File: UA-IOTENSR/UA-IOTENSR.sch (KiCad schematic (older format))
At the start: 4 parts, among them SW101 SW_MEC_5G, U101 ESP32-S2-WROOM, U102 SCD4X

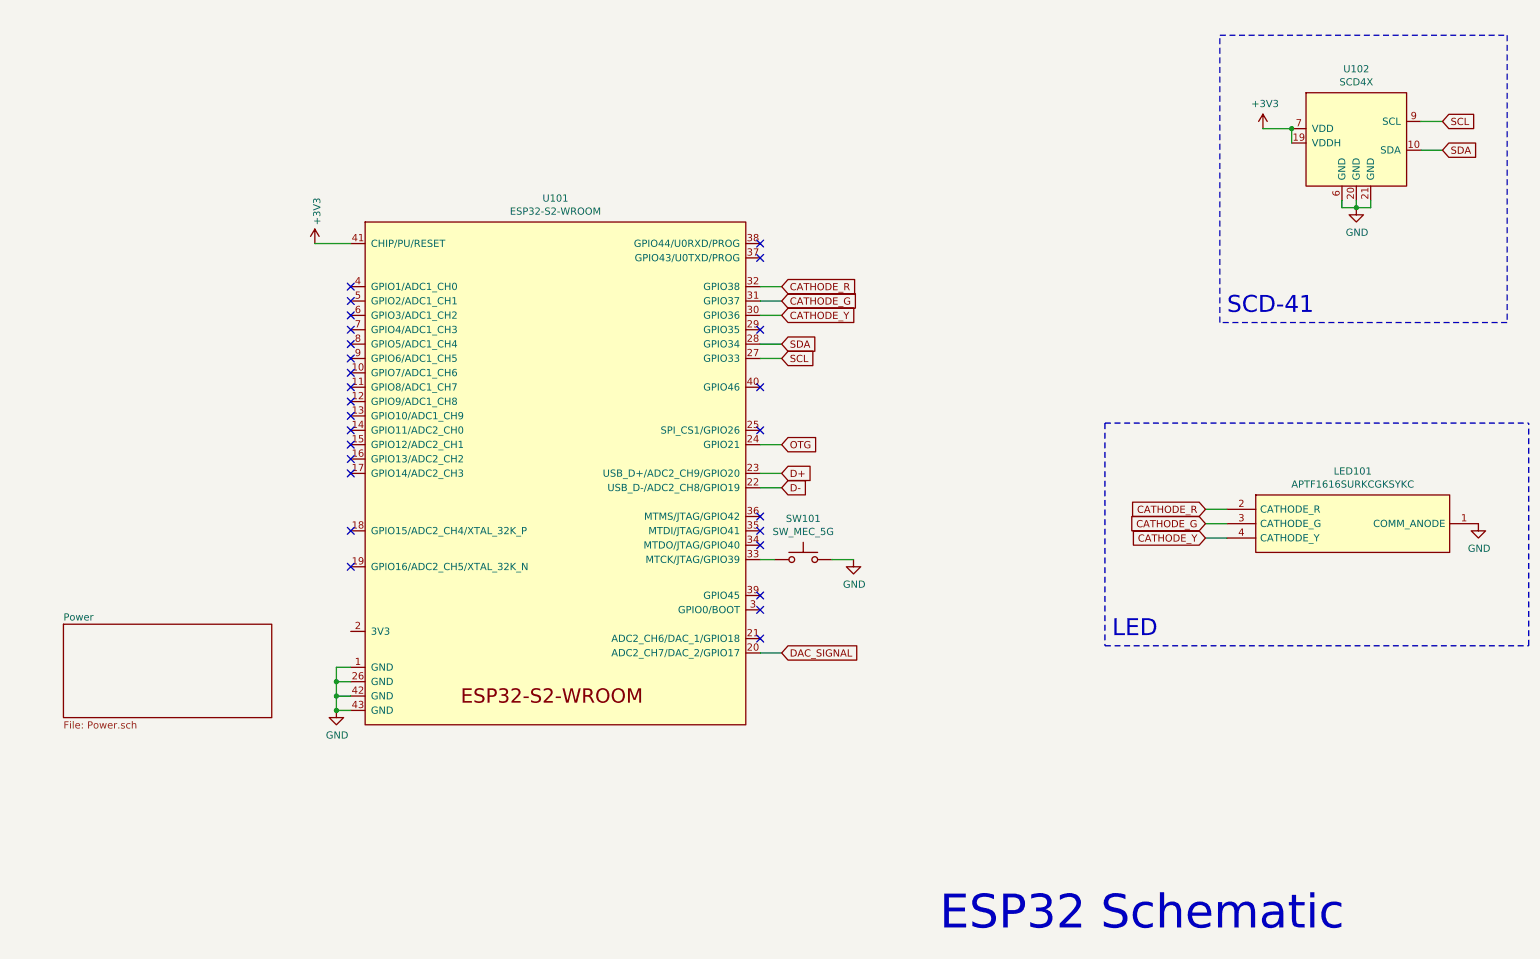
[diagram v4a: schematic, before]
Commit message: Adding footprints; Updated to ESP32-S3-MINI
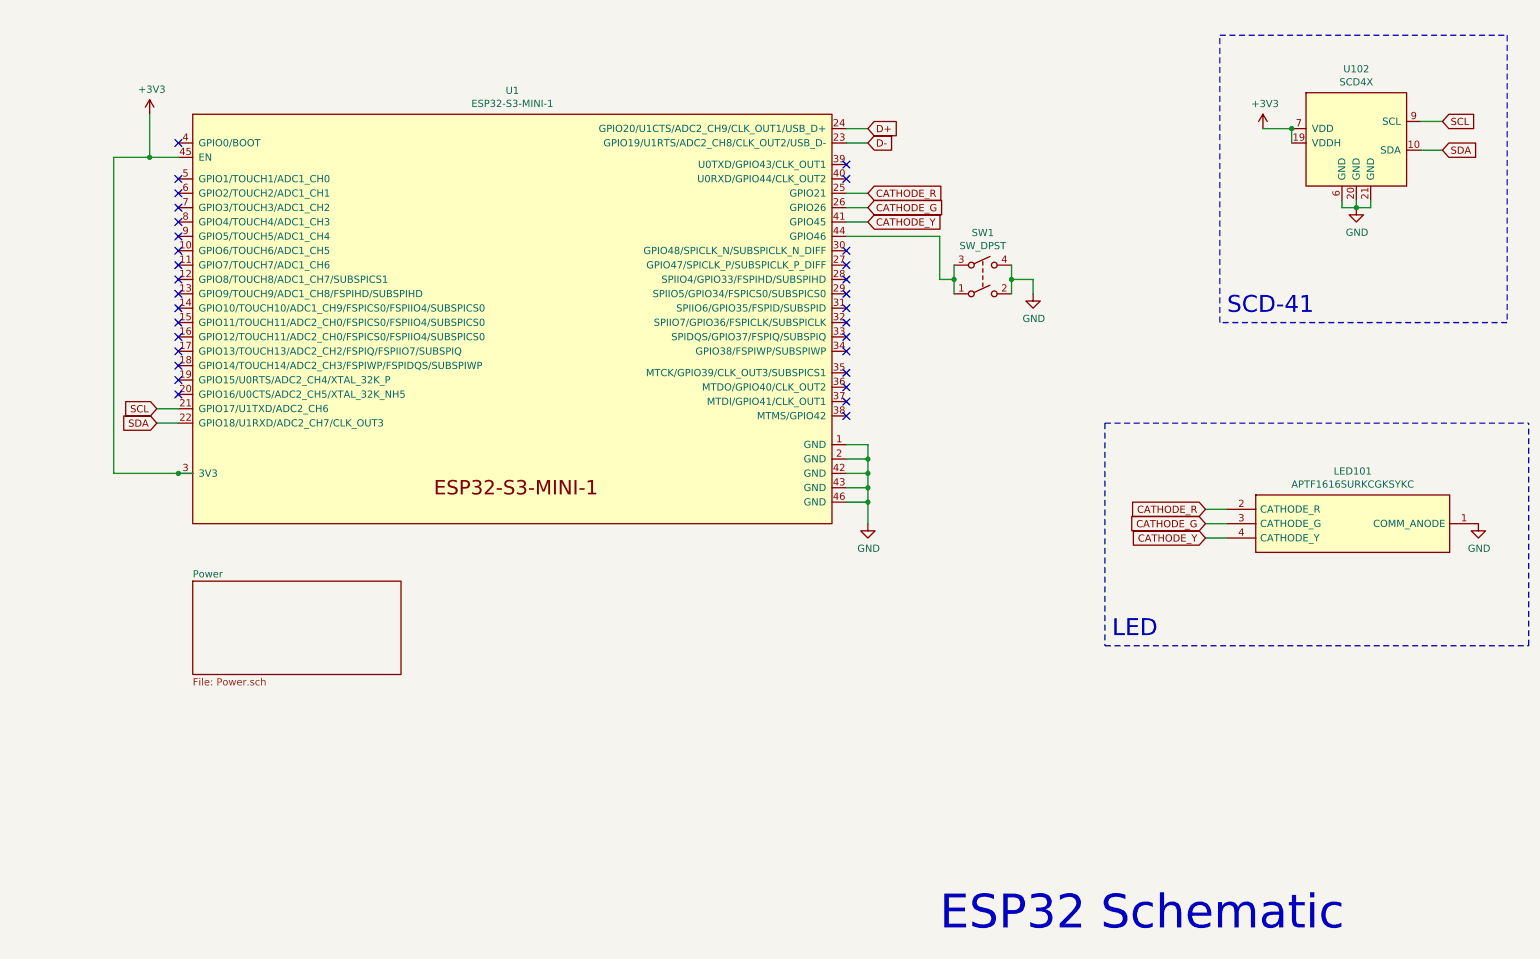
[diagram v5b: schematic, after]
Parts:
- removed SW101: SW_MEC_5G, symbol Switch:SW_MEC_5G
- removed U101: ESP32-S2-WROOM, Espressif:ESP32-S2-WROOM, symbol Espressif:ESP32-S2-WROOM
- added SW1: SW_DPST, SamacSys_Parts2:PB400EEQR1BLK, symbol Switch:SW_DPST
- added U1: ESP32-S3-MINI-1, Espressif:ESP32-S3-MINI-1, symbol Espressif:ESP32-S3-MINI-1
- LED101: footprint KPTF1616RGBC11 -> SamacSys_Parts:KPTF1616RGBC11
- U102: footprint (none) -> Connector_PinSocket_2.54mm:PinSocket_1x04_P2.54mm_Vertical
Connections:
- net +3V3: now also U1.3 (3V3), U1.45 (EN)
- net CATHODE_G: now also U1.26 (GPIO26)
- net CATHODE_R: now also U1.25 (GPIO21)
- net CATHODE_Y: now also U1.41 (GPIO45)
- net D+: now also U1.24 (GPIO20/U1CTS/ADC2_CH9/CLK_OUT1/USB_D+)
- net D-: now also U1.23 (GPIO19/U1RTS/ADC2_CH8/CLK_OUT2/USB_D-)
- net GND: now also SW1.2, SW1.4, U1.1 (GND), U1.2 (GND), U1.42 (GND), U1.43 (GND), U1.46 (GND)
- net SCL: now also U1.21 (GPIO17/U1TXD/ADC2_CH6)
- net SDA: now also U1.22 (GPIO18/U1RXD/ADC2_CH7/CLK_OUT3)
- new net: SW1.1, SW1.3, U1.44 (GPIO46)
- no-connect marks 27 -> 31
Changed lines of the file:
@@
 Comment4 ""
 $EndDescr
-$Comp
-L power:GND #PWR0102
-U 1 1 61961638
-P 2800 5450
-F 0 "#PWR0102" H 2800 5200 50  0001 C CNN
-F 1 "GND" H 2805 5277 50  0000 C CNN
-F 2 "" H 2800 5450 50  0001 C CNN
-F 3 "" H 2800 5450 50  0001 C CNN
-	1    2800 5450
-	1    0    0    -1
-$EndComp
-Wire Wire Line
-	2800 5250 2900 5250
-Wire Wire Line
-	2800 5350 2900 5350
-Wire Wire Line
-	2800 5450 2900 5450
-$Comp
-L Espressif:ESP32-S2-WROOM U101
-U 1 1 619E5D94
-P 4300 3800
-F 0 "U101" H 4325 5715 50  0000 C CNN
-F 1 "ESP32-S2-WROOM" H 4325 5624 50  0000 C CNN
-F 2 "Espressif:ESP32-S2-WROOM" H 4300 1900 50  0001 C CNN
-F 3 "https://www.espressif.com/sites/default/files/documentation/esp32-s2-wroom_esp32-s2-wroom-i_datasheet_en.pdf" H 4300 3800 50  0001 C CNN
-	1    4300 3800
-	1    0    0    -1
-$EndComp
-Wire Wire Line
-	2900 5150 2800 5150
-Wire Wire Line
-	2800 5150 2800 5250
-Connection ~ 2800 5250
-Wire Wire Line
-	2800 5250 2800 5350
-Connection ~ 2800 5350
-Wire Wire Line
-	2800 5350 2800 5450
-Connection ~ 2800 5450
-Wire Wire Line
-	5750 3000 5900 3000
-Text GLabel 5900 3000 2    50   Input ~ 0
+Wire Wire Line
+	1700 3350 1550 3350
+Text GLabel 1550 3350 0    50   Input ~ 0
 SCL
-Text GLabel 5900 2900 2    50   Input ~ 0
+Text GLabel 1550 3450 0    50   Input ~ 0
 SDA
 Wire Wire Line
-	5750 2900 5900 2900
-Wire Wire Line
-	6250 4400 6400 4400
-$Comp
-L Switch:SW_MEC_5G SW101
-U 1 1 619D98CD
-P 6050 4400
-F 0 "SW101" H 6050 4685 50  0000 C CNN
-F 1 "SW_MEC_5G" H 6050 4594 50  0000 C CNN
-F 2 "" H 6050 4600 50  0001 C CNN
-F 3 "http://www.apem.com/int/index.php?controller=attachment&id_attachment=488" H 6050 4600 50  0001 C CNN
-	1    6050 4400
-	1    0    0    -1
-$EndComp
-Wire Wire Line
-	5750 4400 5850 4400
-$Comp
-L power:GND #PWR0103
-U 1 1 61A04BEB
-P 6400 4400
-F 0 "#PWR0103" H 6400 4150 50  0001 C CNN
-F 1 "GND" H 6405 4227 50  0000 C CNN
-F 2 "" H 6400 4400 50  0001 C CNN
-F 3 "" H 6400 4400 50  0001 C CNN
-	1    6400 4400
-	1    0    0    -1
-$EndComp
-Text GLabel 5900 3800 2    50   Input ~ 0
+	1700 3450 1550 3450
+Text GLabel 6500 1400 2    50   Input ~ 0
 D+
 Wire Wire Line
-	5750 3800 5900 3800
-Text GLabel 5900 3900 2    50   Input ~ 0
+	6350 1400 6500 1400
+Text GLabel 6500 1500 2    50   Input ~ 0
 D-
 Wire Wire Line
-	5750 3900 5900 3900
-Wire Wire Line
-	5750 3600 5900 3600
-Text GLabel 5900 3600 2    50   Input ~ 0
-OTG
+	6350 1500 6500 1500
 $Sheet
-S 900  4850 1450 650
+S 1800 4550 1450 650
 U 61A2F8E2
 F0 "Power" 50
 F1 "Power.sch" 50
 $EndSheet
-NoConn ~ 5750 4950
-NoConn ~ 5750 4750
-NoConn ~ 5750 4650
-NoConn ~ 5750 4300
-NoConn ~ 5750 4200
-NoConn ~ 5750 4100
-NoConn ~ 5750 3500
-NoConn ~ 5750 3200
-NoConn ~ 5750 2800
-NoConn ~ 5750 2300
-NoConn ~ 5750 2200
-NoConn ~ 2900 2500
-NoConn ~ 2900 2600
-NoConn ~ 2900 2700
-NoConn ~ 2900 2800
-NoConn ~ 2900 2900
-NoConn ~ 2900 3000
-NoConn ~ 2900 3100
-NoConn ~ 2900 3200
-NoConn ~ 2900 3300
-NoConn ~ 2900 3400
-NoConn ~ 2900 3500
-NoConn ~ 2900 3600
-NoConn ~ 2900 3700
-NoConn ~ 2900 3800
-NoConn ~ 2900 4200
-NoConn ~ 2900 4450
 Text Notes 7000 7000 0    236  ~ 0
 ESP32 Schematic
-$Comp
-L power:+3V3 #PWR0101
-U 1 1 61A18D2A
-P 2650 2200
-F 0 "#PWR0101" H 2650 2050 50  0001 C CNN
-F 1 "+3V3" V 2665 2328 50  0000 L CNN
-F 2 "" H 2650 2200 50  0001 C CNN
-F 3 "" H 2650 2200 50  0001 C CNN
-	1    2650 2200
-	1    0    0    -1
-$EndComp
-Text GLabel 5900 5050 2    50   Input ~ 0
-DAC_SIGNAL
-Wire Wire Line
-	5750 5050 5900 5050
-Wire Wire Line
-	2900 2200 2650 2200
 $Comp
 L SCD4X:SCD4X U102
@@
 F 0 "U102" H 9900 1915 50  0000 C CNN
 F 1 "SCD4X" H 9900 1824 50  0000 C CNN
-F 2 "" H 9900 1900 50  0001 C CNN
+F 2 "Connector_PinSocket_2.54mm:PinSocket_1x04_P2.54mm_Vertical" H 9900 1900 50  0001 C CNN
 F 3 "" H 9900 1900 50  0001 C CNN
 	1    9900 1450
@@
 F 0 "LED101" H 9875 4315 50  0000 C CNN
 F 1 "APTF1616SURKCGKSYKC" H 9875 4224 50  0000 C CNN
-F 2 "KPTF1616RGBC11" H 10950 4150 50  0001 L CNN
+F 2 "SamacSys_Parts:KPTF1616RGBC11" H 10950 4150 50  0001 L CNN
 F 3 "" H 9150 3850 50  0001 L CNN
 F 4 "Standard LEDs - SMD RGY 1616 SMD" H 11150 3850 50  0001 L CNN "Description"
@@
 	8150 3450 8150 5000
 Wire Wire Line
-	5750 2600 5900 2600
-Text GLabel 5900 2600 2    50   Input ~ 0
+	6350 1950 6500 1950
+Text GLabel 6500 1950 2    50   Input ~ 0
 CATHODE_G
-Text GLabel 5900 2500 2    50   Input ~ 0
+Text GLabel 6500 1850 2    50   Input ~ 0
 CATHODE_R
 Wire Wire Line
-	5750 2500 5900 2500
-Wire Wire Line
-	5750 2700 5900 2700
-Text GLabel 5900 2700 2    50   Input ~ 0
+	6350 1850 6500 1850
+Wire Wire Line
+	6350 2050 6500 2050
+Text GLabel 6500 2050 2    50   Input ~ 0
 CATHODE_Y
 Wire Wire Line
@@
 Wire Notes Line
 	8150 5000 11100 5000
+Wire Wire Line
+	7000 2450 7100 2450
+Wire Wire Line
+	6350 2150 7000 2150
+Wire Wire Line
+	6350 3600 6500 3600
+Wire Wire Line
+	6500 3600 6500 3700
+Wire Wire Line
+	6500 4000 6350 4000
+Wire Wire Line
+	6350 3900 6500 3900
+Connection ~ 6500 3900
+Wire Wire Line
+	6500 3900 6500 4000
+Wire Wire Line
+	6350 3800 6500 3800
+Connection ~ 6500 3800
+Wire Wire Line
+	6500 3800 6500 3900
+Wire Wire Line
+	6350 3700 6500 3700
+Connection ~ 6500 3700
+Wire Wire Line
+	6500 3700 6500 3800
+Wire Wire Line
+	6500 4000 6500 4150
+Connection ~ 6500 4000
+$Comp
+L power:GND #PWR0101
+U 1 1 62086CA7
+P 6500 4150
+F 0 "#PWR0101" H 6500 3900 50  0001 C CNN
+F 1 "GND" H 6505 3977 50  0000 C CNN
+F 2 "" H 6500 4150 50  0001 C CNN
+F 3 "" H 6500 4150 50  0001 C CNN
+	1    6500 4150
+	1    0    0    -1
+$EndComp
+$Comp
+L power:+3V3 #PWR0102
+U 1 1 6208B06F
+P 1500 1300
+F 0 "#PWR0102" H 1500 1150 50  0001 C CNN
+F 1 "+3V3" H 1515 1473 50  0000 C CNN
+F 2 "" H 1500 1300 50  0001 C CNN
+F 3 "" H 1500 1300 50  0001 C CNN
+	1    1500 1300
+	1    0    0    -1
+$EndComp
+Wire Wire Line
+	1700 1600 1500 1600
+Wire Wire Line
+	1500 1600 1500 1300
+$Comp
+L Espressif:ESP32-S3-MINI-1 U1
+U 1 1 6205E07D
+P 4050 2650
+F 0 "U1" H 4025 4165 50  0000 C CNN
+F 1 "ESP32-S3-MINI-1" H 4025 4074 50  0000 C CNN
+F 2 "Espressif:ESP32-S3-MINI-1" H 4050 1000 50  0001 C CNN
+F 3 "" H 4050 2950 50  0001 C CNN
+	1    4050 2650
+	1    0    0    -1
+$EndComp
+NoConn ~ 1700 1500
+NoConn ~ 1700 1750
+NoConn ~ 1700 1850
+NoConn ~ 1700 1950
+NoConn ~ 1700 2050
+NoConn ~ 1700 2150
+NoConn ~ 1700 2250
+NoConn ~ 1700 2350
+NoConn ~ 1700 2450
+NoConn ~ 1700 2550
+NoConn ~ 1700 2650
+NoConn ~ 1700 2750
+NoConn ~ 1700 2850
+NoConn ~ 1700 2950
+NoConn ~ 1700 3050
+NoConn ~ 1700 3150
+NoConn ~ 1700 3250
+Connection ~ 1700 3800
+Wire Wire Line
+	1700 3800 1800 3800
+Wire Wire Line
+	1250 3800 1700 3800
+Wire Wire Line
+	1250 3800 1250 1600
+Wire Wire Line
+	1250 1600 1500 1600
+Connection ~ 1500 1600
+$Comp
+L Switch:SW_DPST SW1
+U 1 1 620C5E9D
+P 7300 2450
+F 0 "SW1" H 7300 2775 50  0000 C CNN
+F 1 "SW_DPST" H 7300 2684 50  0000 C CNN
+F 2 "SamacSys_Parts2:PB400EEQR1BLK" H 7300 2450 50  0001 C CNN
+F 3 "~" H 7300 2450 50  0001 C CNN
+	1    7300 2450
+	1    0    0    -1
+$EndComp
+Wire Wire Line
+	7100 2550 7100 2450
+Wire Wire Line
+	7500 2550 7500 2450
+Wire Wire Line
+	7500 2450 7650 2450
+Wire Wire Line
+	7650 2450 7650 2550
+Connection ~ 7500 2450
+Wire Wire Line
+	7500 2450 7500 2350
+Connection ~ 7100 2450
+Wire Wire Line
+	7100 2450 7100 2350
+Wire Wire Line
+	7000 2150 7000 2450
+$Comp
+L power:GND #PWR0103
+U 1 1 620D10AA
+P 7650 2550
+F 0 "#PWR0103" H 7650 2300 50  0001 C CNN
+F 1 "GND" H 7655 2377 50  0000 C CNN
+F 2 "" H 7650 2550 50  0001 C CNN
+F 3 "" H 7650 2550 50  0001 C CNN
+	1    7650 2550
+	1    0    0    -1
+$EndComp
+NoConn ~ 6350 3400
+NoConn ~ 6350 3300
+NoConn ~ 6350 3200
+NoConn ~ 6350 3100
+NoConn ~ 6350 2950
+NoConn ~ 6350 2850
+NoConn ~ 6350 2750
+NoConn ~ 6350 2650
+NoConn ~ 6350 2550
+NoConn ~ 6350 2450
+NoConn ~ 6350 2350
+NoConn ~ 6350 2250
+NoConn ~ 6350 1750
+NoConn ~ 6350 1650
 $EndSCHEMATC

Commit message: All resistor and inductor footprints attached (except RTx)
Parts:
- SW1: footprint SamacSys_Parts2:PB400EEQR1BLK -> SamacSys_Parts:PB400EEQR1BLK
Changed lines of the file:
@@
 F 0 "SW1" H 7300 2775 50  0000 C CNN
 F 1 "SW_DPST" H 7300 2684 50  0000 C CNN
-F 2 "SamacSys_Parts2:PB400EEQR1BLK" H 7300 2450 50  0001 C CNN
+F 2 "SamacSys_Parts:PB400EEQR1BLK" H 7300 2450 50  0001 C CNN
 F 3 "~" H 7300 2450 50  0001 C CNN
 	1    7300 2450
